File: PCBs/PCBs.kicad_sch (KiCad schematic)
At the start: 18 parts, among them J3 USB_C_Receptacle_USB2.0_14P, U1 STM32L476RGTx, U2 MPU-9250, U4 USBLC6-2P6, U6 TPS62131, U7 TPS62172DSG

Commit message: trace
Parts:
- BuckConverter3-17V->3.3V-C1: footprint (none) -> Capacitor_Tantalum_SMD:CP_EIA-1608-10_AVX-L
- BuckConverter3-17V->3.3V-C2: renamed from 22uF; value BuckConverter3-17V->3.3V-C2 -> 22uF; footprint (none) -> Capacitor_Tantalum_SMD:CP_EIA-1608-10_AVX-L
- BuckConverter3-17V->3.3V-L1: renamed from L1; footprint (none) -> Inductor_SMD:L_0201_0603Metric_Pad0.64x0.40mm_HandSolder
- BuckConverter3-17V->3.3V-LED1: renamed from BuckConverter3-17V->3.3V-LED; value Green -> LED; footprint (none) -> LED_SMD:LED_0201_0603Metric_Pad0.64x0.40mm_HandSolder
- BuckConverter3-17V->3.3V-R1: value 1k Ohms -> 100k Ohms; footprint (none) -> Resistor_SMD:R_0402_1005Metric_Pad0.72x0.64mm_HandSolder
- renumbered C2 to C1, C1 to C2, J3 to J1, U3 to U2, U2 to U3, U6 to U5, U7 to U6
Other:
- moved on the sheet: BuckConverter3-17V->3.3V-C2

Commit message: buck converter
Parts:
- added BuckConverter3-17V->3.3V-ScrewTerminalInput1: Input, TerminalBlock_4Ucon:TerminalBlock_4Ucon_1x02_P3.50mm_Horizontal, symbol Connector:Screw_Terminal_01x02
- added BuckConverter3-17V->3.3V-ScrewTerminalOutput1: Output, TerminalBlock_4Ucon:TerminalBlock_4Ucon_1x02_P3.50mm_Horizontal, symbol Connector:Screw_Terminal_01x02
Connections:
- net VCC: no longer BuckConverter3-17V->3.3V-C1.1, BuckConverter3-17V->3.3V-C2.2, BuckConverter3-17V->3.3V-L1.2, BuckConverter3-17V->3.3V-R1.2, U6.2 (VIN), U6.3 (EN), U6.6 (VOS)
- new net VCCIN: BuckConverter3-17V->3.3V-C1.1, U6.2 (VIN), U6.3 (EN)
- new net VCCOUT: BuckConverter3-17V->3.3V-C2.2, BuckConverter3-17V->3.3V-L1.2, BuckConverter3-17V->3.3V-R1.2, U6.6 (VOS)
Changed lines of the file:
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@@
-	(wire
-		(pts
-			(xy 205.74 72.39) (xy 205.74 80.01)
-		)
-		(stroke
-			(width 0)
-			(type default)
-		)
-	)
 	(wire
 		(pts
@@
 			)
 		)
-		(property "Value" "VCC"
+		(property "Value" "VCCOUT"
 			(at 135.89 109.982 0)
 			(effects
@@
 	)
 	(symbol
+		(lib_id "Connector:Screw_Terminal_01x02")
+		(at 128.27 68.58 0)
+		(unit 1)
+		(exclude_from_sim no)
+		(in_bom yes)
+		(on_board yes)
+		(dnp no)
+		(property "Reference" "BuckConverter3-17V->3.3V-ScrewTerminalInput1"
+			(at 109.474 65.786 0)
+			(effects
+				(font
+					(size 1.27 1.27)
+				)
+				(justify left)
+			)
+		)
+		(property "Value" "Input"
+			(at 130.81 71.1199 0)
+			(effects
+				(font
+					(size 1.27 1.27)
+				)
+				(justify left)
+				(hide yes)
+			)
+		)
+		(property "Footprint" "TerminalBlock_4Ucon:TerminalBlock_4Ucon_1x02_P3.50mm_Horizontal"
+			(at 128.27 68.58 0)
+			(effects
+				(font
+					(size 1.27 1.27)
+				)
+				(hide yes)
+			)
+		)
+		(property "Datasheet" "~"
+			(at 128.27 68.58 0)
+			(effects
+				(font
+					(size 1.27 1.27)
+				)
+				(hide yes)
+			)
+		)
+		(property "Description" "Generic screw terminal, single row, 01x02, script generated (kicad-library-utils/schlib/autogen/connector/)"
+			(at 128.27 68.58 0)
+			(effects
+				(font
+					(size 1.27 1.27)
+				)
+				(hide yes)
+			)
+		)
+		(pin "1"
+		)
+		(pin "2"
+		)
+		(instances
+			(project ""
+				(path "/d221d146-1e04-473b-9f27-373863f06afb"
+					(reference "BuckConverter3-17V->3.3V-ScrewTerminalInput1")
+					(unit 1)
+				)
+			)
+		)
+	)
+	(symbol
 		(lib_id "Device:R_Small_US")
 		(at 137.16 105.41 0)
@@
 	)
 	(symbol
+		(lib_id "Connector:Screw_Terminal_01x02")
+		(at 180.34 68.58 0)
+		(unit 1)
+		(exclude_from_sim no)
+		(in_bom yes)
+		(on_board yes)
+		(dnp no)
+		(property "Reference" "BuckConverter3-17V->3.3V-ScrewTerminalOutput1"
+			(at 161.544 65.786 0)
+			(effects
+				(font
+					(size 1.27 1.27)
+				)
+				(justify left)
+			)
+		)
+		(property "Value" "Output"
+			(at 182.88 71.1199 0)
+			(effects
+				(font
+					(size 1.27 1.27)
+				)
+				(justify left)
+				(hide yes)
+			)
+		)
+		(property "Footprint" "TerminalBlock_4Ucon:TerminalBlock_4Ucon_1x02_P3.50mm_Horizontal"
+			(at 180.34 68.58 0)
+			(effects
+				(font
+					(size 1.27 1.27)
+				)
+				(hide yes)
+			)
+		)
+		(property "Datasheet" "~"
+			(at 180.34 68.58 0)
+			(effects
+				(font
+					(size 1.27 1.27)
+				)
+				(hide yes)
+			)
+		)
+		(property "Description" "Generic screw terminal, single row, 01x02, script generated (kicad-library-utils/schlib/autogen/connector/)"
+			(at 180.34 68.58 0)
+			(effects
+				(font
+					(size 1.27 1.27)
+				)
+				(hide yes)
+			)
+		)
+		(pin "1"
+		)
+		(pin "2"
+		)
+		(instances
+			(project "PCBs"
+				(path "/d221d146-1e04-473b-9f27-373863f06afb"
+					(reference "BuckConverter3-17V->3.3V-ScrewTerminalOutput1")
+					(unit 1)
+				)
+			)
+		)
+	)
+	(symbol
 		(lib_id "power:GND")
 		(at 139.7 -81.28 0)
@@
 			)
 		)
-		(property "Value" "VCC"
+		(property "Value" "VCCIN"
 			(at 132.842 87.63 90)
 			(effects
@@
 			)
 		)
-		(property "Value" "VCC"
+		(property "Value" "VCCOUT"
 			(at 169.418 87.63 90)
 			(effects

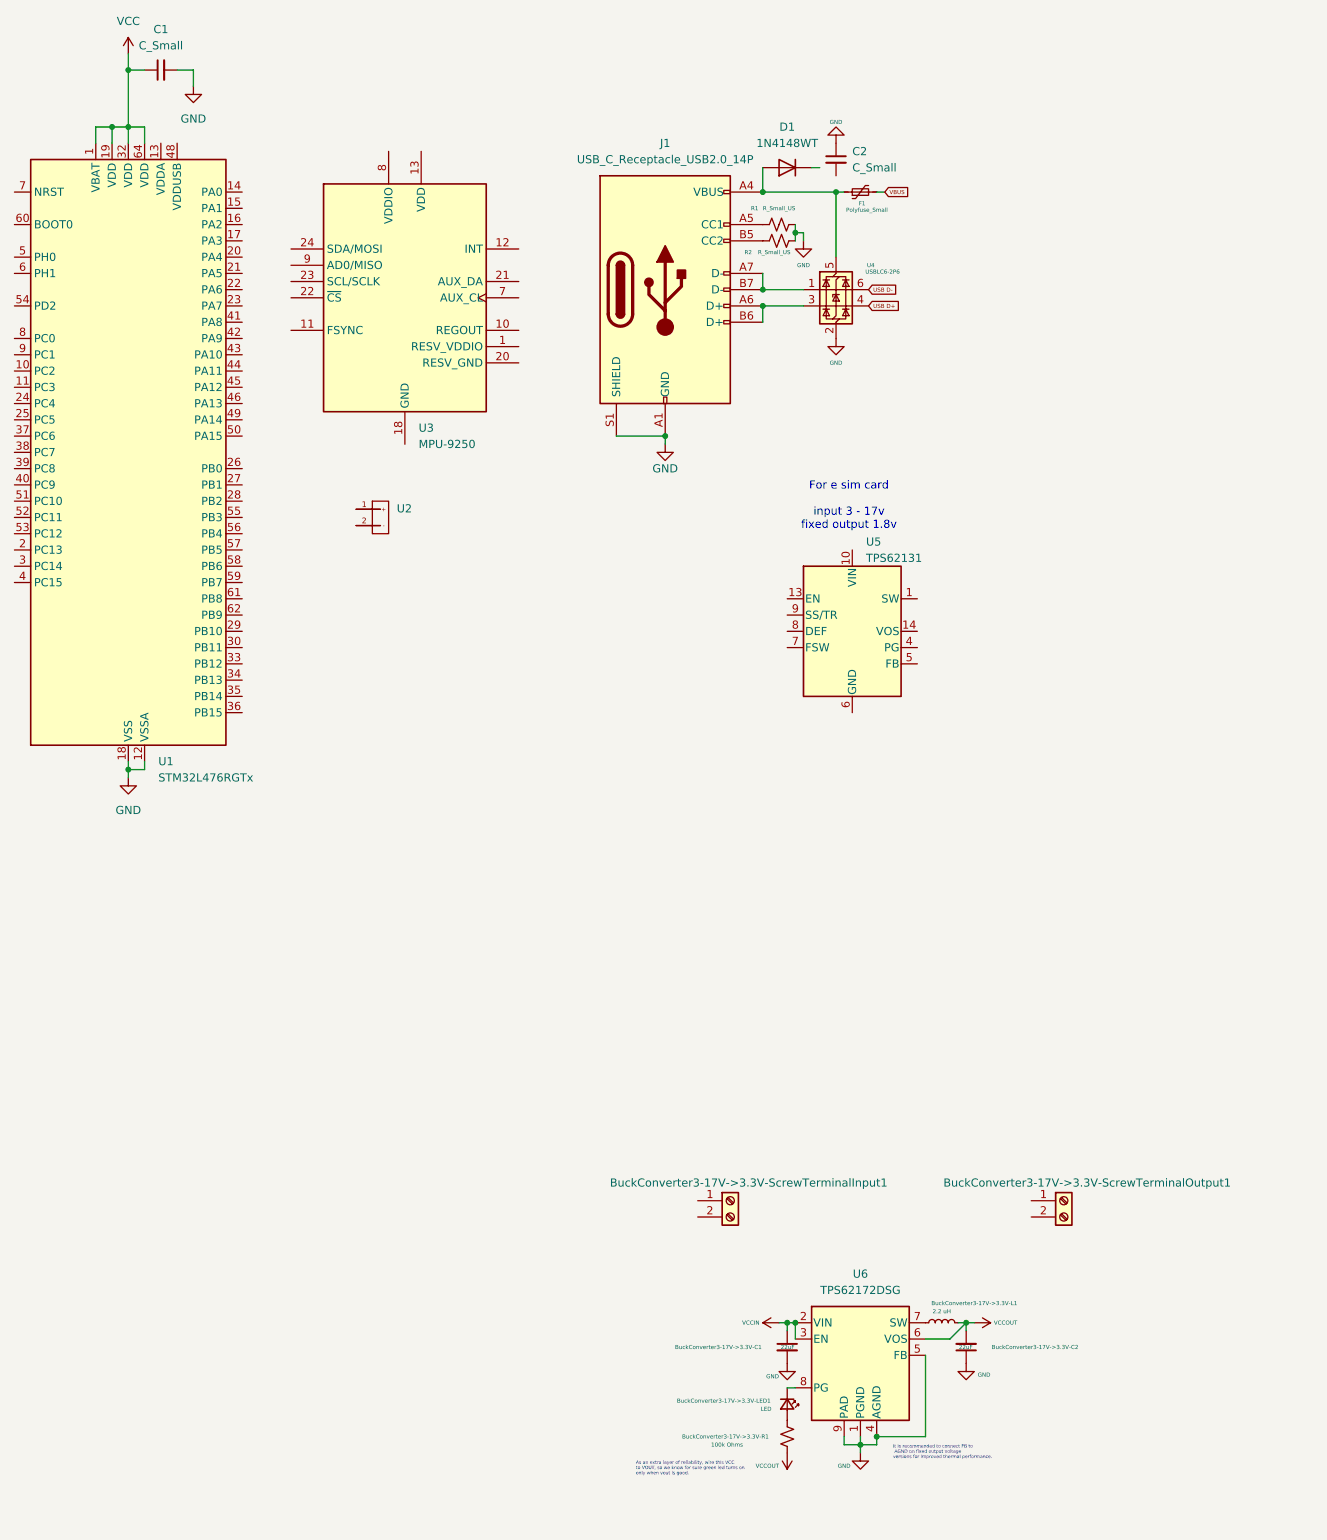
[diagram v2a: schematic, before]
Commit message: changes for easyeda components
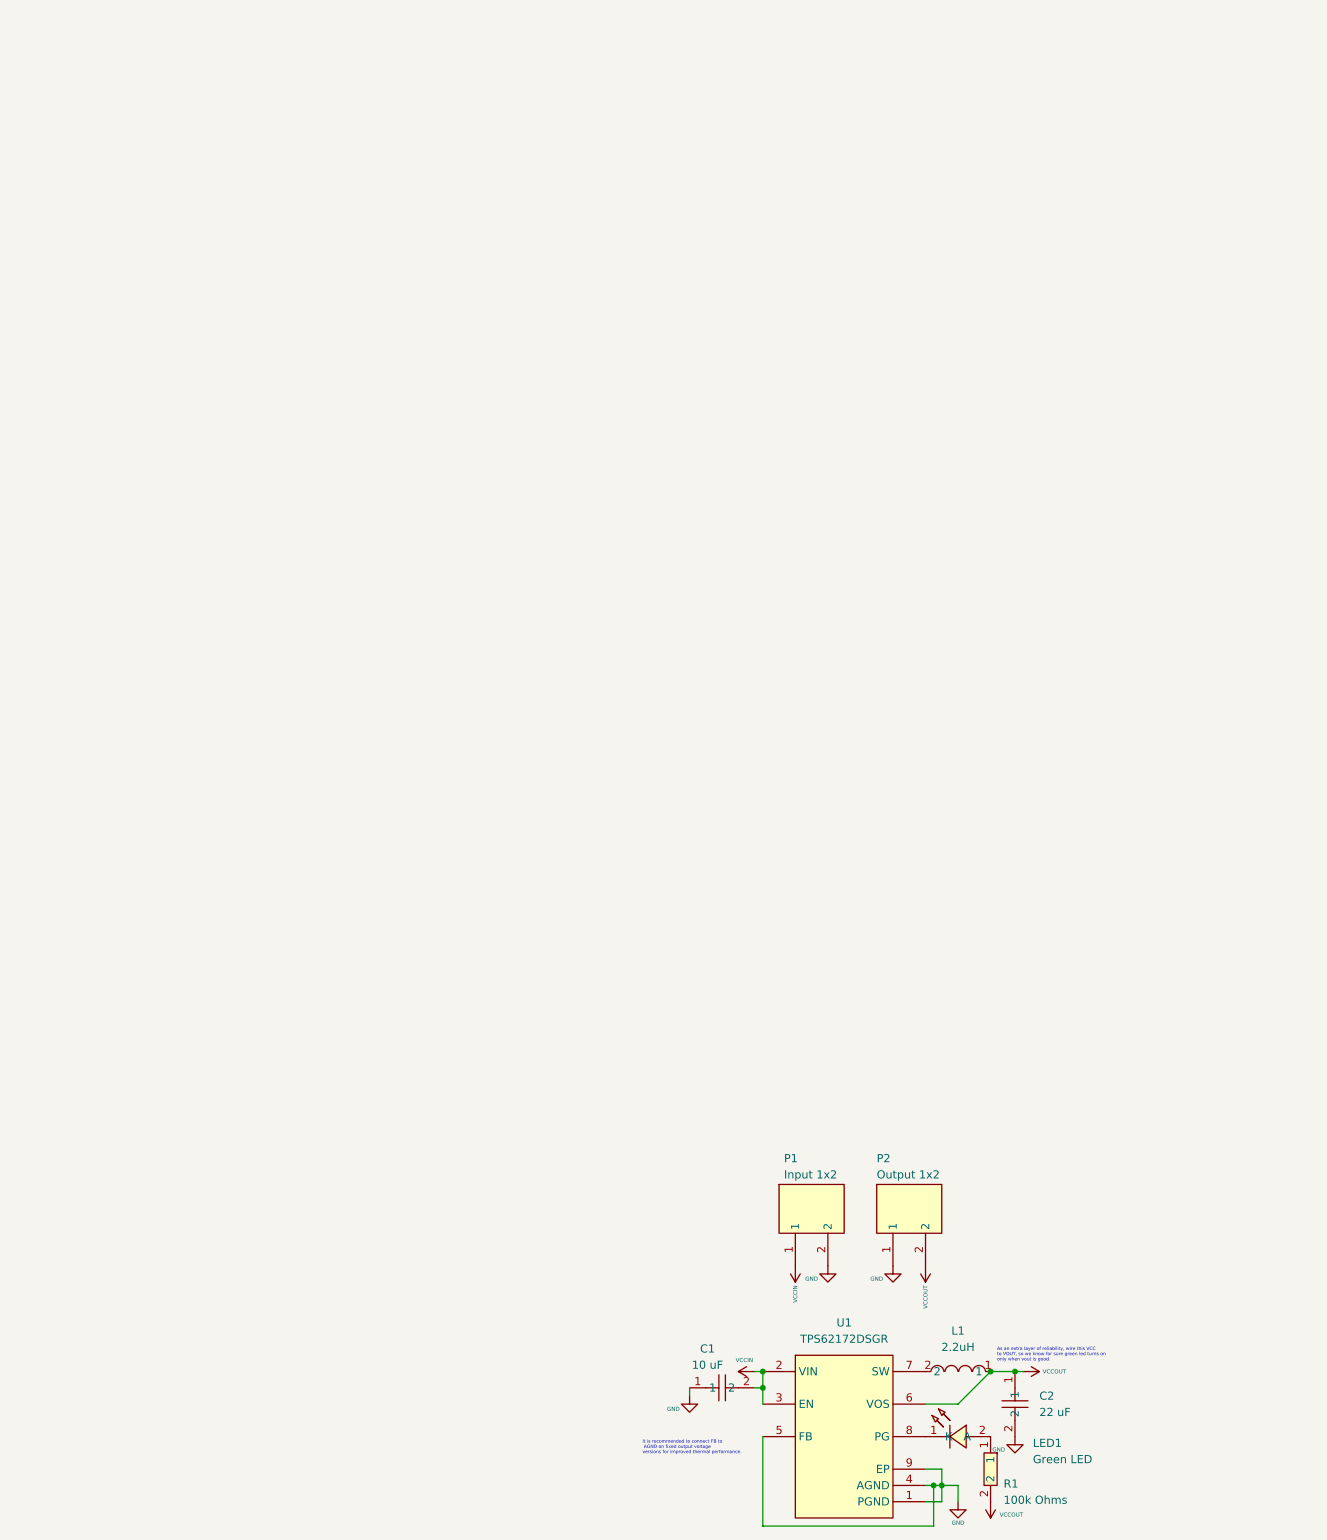
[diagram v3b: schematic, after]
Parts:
- removed BuckConverter3-17V->3.3V-C1, BuckConverter3-17V->3.3V-C2: 22uF, Capacitor_Tantalum_SMD:CP_EIA-1608-10_AVX-L, symbol Device:C_Small
- removed BuckConverter3-17V->3.3V-L1: 2.2 uH, Inductor_SMD:L_0201_0603Metric_Pad0.64x0.40mm_HandSolder, symbol Device:L_Small
- removed BuckConverter3-17V->3.3V-LED1: LED, LED_SMD:LED_0201_0603Metric_Pad0.64x0.40mm_HandSolder, symbol Device:LED_Small
- removed BuckConverter3-17V->3.3V-R1: 100k Ohms, Resistor_SMD:R_0402_1005Metric_Pad0.72x0.64mm_HandSolder, symbol Device:R_Small_US
- removed BuckConverter3-17V->3.3V-ScrewTerminalInput1: Input, TerminalBlock_4Ucon:TerminalBlock_4Ucon_1x02_P3.50mm_Horizontal, symbol Connector:Screw_Terminal_01x02
- removed BuckConverter3-17V->3.3V-ScrewTerminalOutput1: Output, TerminalBlock_4Ucon:TerminalBlock_4Ucon_1x02_P3.50mm_Horizontal, symbol Connector:Screw_Terminal_01x02
- removed C1, C2: C_Small, symbol Device:C_Small
- removed D1: 1N4148WT, Diode_SMD:D_SOD-523, symbol Diode:1N4148WT
- removed F1: Polyfuse_Small, symbol Device:Polyfuse_Small
- removed J1: USB_C_Receptacle_USB2.0_14P, symbol Connector:USB_C_Receptacle_USB2.0_14P
- removed R1, R2: R_Small_US, symbol Device:R_Small_US
- removed U1: STM32L476RGTx, Package_QFP:LQFP-64_10x10mm_P0.5mm, symbol MCU_ST_STM32L4:STM32L476RGTx
- removed U2: ~, Connector_JST:JST_PH_B2B-PH-K_1x02_P2.00mm_Vertical, symbol Custom_Library:1x2_Battery_Connector
- removed U3: MPU-9250, Sensor_Motion:InvenSense_QFN-24_3x3mm_P0.4mm, symbol Sensor_Motion:MPU-9250
- removed U4: USBLC6-2P6, Package_TO_SOT_SMD:SOT-666, symbol Power_Protection:USBLC6-2P6
- removed U5: TPS62131, Package_DFN_QFN:VQFN-16-1EP_3x3mm_P0.5mm_EP1.68x1.68mm_ThermalVias, symbol Regulator_Switching:TPS62131
- removed U6: TPS62172DSG, Package_SON:WSON-8-1EP_2x2mm_P0.5mm_EP0.9x1.6mm_ThermalVias, symbol Regulator_Switching:TPS62172DSG
- added C1: 10 uF, EasyEDA2KicadFootprints:C0603, symbol EasyEDA2KicadSymbols:CL10A106MQ8NNNC
- added C2: 22 uF, EasyEDA2KicadFootprints:C0805, symbol EasyEDA2KicadSymbols:CL21A226MQQNNNE
- added L1: 2.2uH, EasyEDA2KicadFootprints:IND-SMD_L4.0-W4.0_LQH44PN2R2MP0L, symbol EasyEDA2KicadSymbols:SMNR4020-2.2UH
- added LED1: Green LED, EasyEDA2KicadFootprints:LED-SMD_L0.7-W0.4-RD_GREEN, symbol EasyEDA2KicadSymbols:XL-0201UGC
- added P1: Input 1x2, EasyEDA2KicadFootprints:CONN-TH_2P-P5.00_WJ128V-5.0-2P, symbol EasyEDA2KicadSymbols:WJ128V-5.0-2P
- added P2: Output 1x2, EasyEDA2KicadFootprints:CONN-TH_2P-P5.00_WJ128V-5.0-2P, symbol EasyEDA2KicadSymbols:WJ128V-5.0-2P
- added R1: 100k Ohms, EasyEDA2KicadFootprints:R0402, symbol EasyEDA2KicadSymbols:QR0402J100KQ10
- added U1: TPS62172DSGR, EasyEDA2KicadFootprints:WSON-8_L2.0-W2.0-P0.50-TL-EP, symbol EasyEDA2KicadSymbols:TPS62172DSGR
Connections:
- net GND: now also C1.1, C2.2, P1.2, P2.1, U1.1 (PGND), U1.4 (AGND), U1.5 (FB), U1.9 (EP)
- net VCCIN: now also C1.2, P1.1, U1.2 (VIN), U1.3 (EN)
- net VCCOUT: now also C2.1, L1.1, P2.2, R1.2, U1.6 (VOS)
- new net: L1.2, U1.7 (SW)
- new net: LED1.1 (K), U1.8 (PG)
- new net: LED1.2 (A), R1.1
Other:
- note removed: "For e sim card input 3 - 17v fixed output 1.8v"
